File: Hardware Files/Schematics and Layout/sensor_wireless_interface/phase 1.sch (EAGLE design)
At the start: 6 parts, among them U1 RHD2216

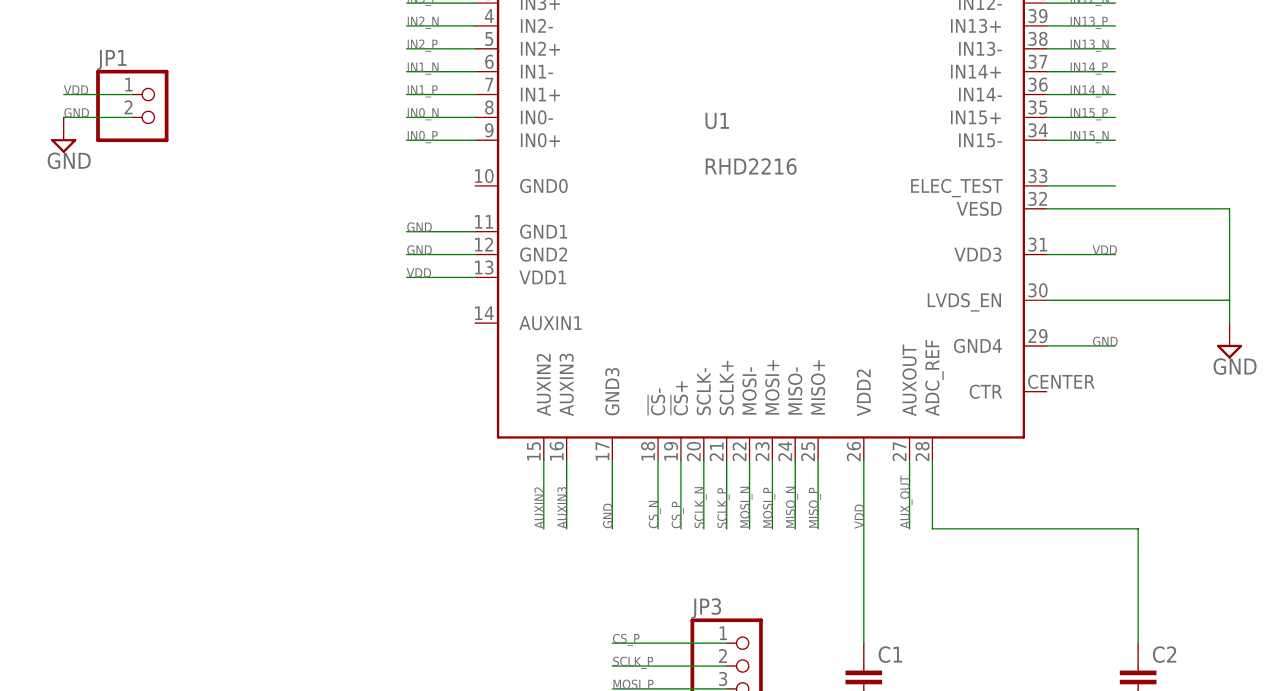
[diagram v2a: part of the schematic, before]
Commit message: added another pin header for AUXIN*
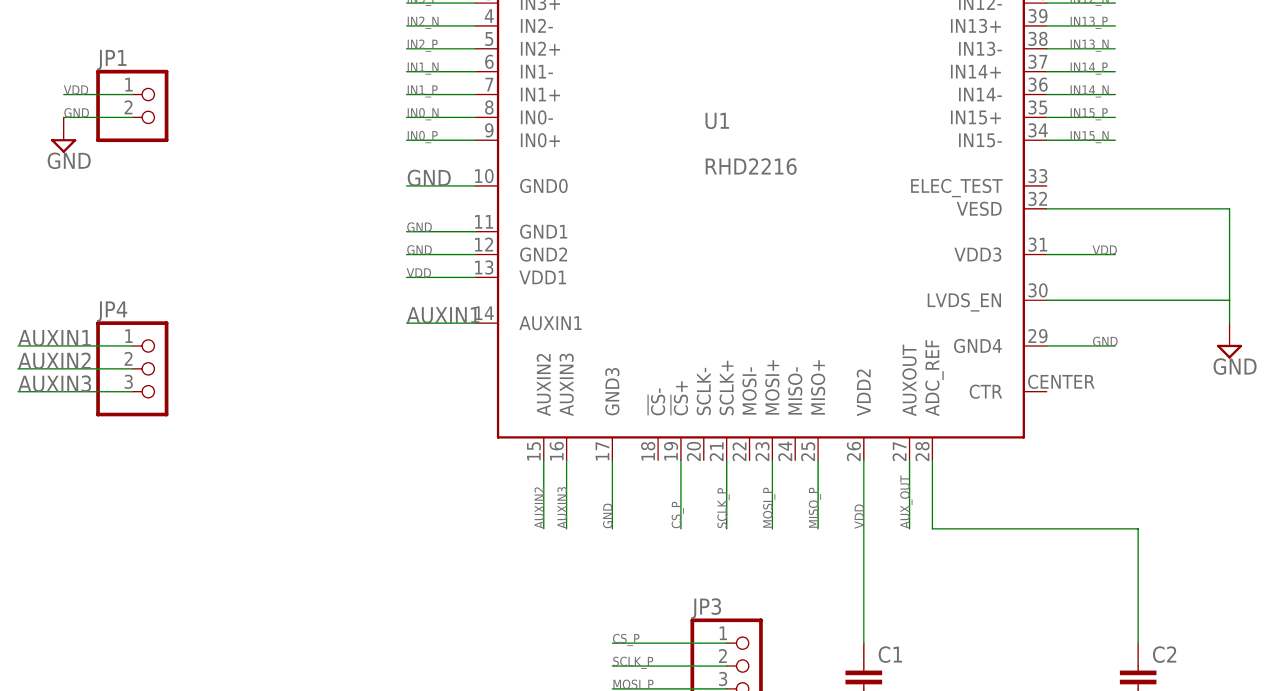
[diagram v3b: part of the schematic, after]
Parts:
- added JP4: (no value), pinhead:PINHD-1X3
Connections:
- removed net CS_N: U1.!CS!-
- removed net MISO_N: U1.MISO-
- removed net MOSI_N: U1.MOSI-
- removed net N$10: U1.ELEC_TEST
- removed net SCLK_N: U1.SCLK-
- new net AUXIN1: JP4.1, U1.AUXIN1
- net AUXIN2: now also JP4.2
- net AUXIN3: now also JP4.3
- net GND: now also U1.GND0
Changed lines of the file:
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@@
 <part name="C2" library="capacitor-wima" deviceset="C" device="2.5/2" value="10nF"/>
 <part name="SUPPLY4" library="supply2" deviceset="GND" device=""/>
+<part name="JP4" library="pinhead" deviceset="PINHD-1X3" device=""/>
 </parts>
 <sheets>
@@
 <instance part="C2" gate="G$1" x="10.16" y="35.56"/>
 <instance part="SUPPLY4" gate="GND" x="10.16" y="27.94"/>
+<instance part="JP4" gate="A" x="-99.06" y="68.58"/>
 </instances>
 <busses>
@@
 <pinref part="SUPPLY4" gate="GND" pin="GND"/>
 </segment>
+<segment>
+<pinref part="U1" gate="A" pin="GND0"/>
+<wire x1="-63.5" y1="88.9" x2="-71.12" y2="88.9" width="0.1524" layer="91"/>
+<label x="-71.12" y="88.9" size="1.778" layer="95"/>
+</segment>
 </net>
 <net name="AUXIN2" class="0">
@@
 <label x="-55.88" y="50.8" size="1.016" layer="95" rot="R90"/>
 </segment>
+<segment>
+<pinref part="JP4" gate="A" pin="2"/>
+<wire x1="-101.6" y1="68.58" x2="-114.3" y2="68.58" width="0.1524" layer="91"/>
+<label x="-114.3" y="68.58" size="1.778" layer="95"/>
+</segment>
 </net>
 <net name="AUXIN3" class="0">
@@
 <label x="-53.34" y="50.8" size="1.016" layer="95" rot="R90"/>
 </segment>
-</net>
-<net name="CS_N" class="0">
-<segment>
-<pinref part="U1" gate="A" pin="!CS!-"/>
-<wire x1="-43.18" y1="58.42" x2="-43.18" y2="50.8" width="0.1524" layer="91"/>
-<label x="-43.18" y="50.8" size="1.016" layer="95" rot="R90"/>
+<segment>
+<pinref part="JP4" gate="A" pin="3"/>
+<wire x1="-101.6" y1="66.04" x2="-114.3" y2="66.04" width="0.1524" layer="91"/>
+<label x="-114.3" y="66.04" size="1.778" layer="95"/>
 </segment>
 </net>
@@
 </segment>
 </net>
-<net name="SCLK_N" class="0">
-<segment>
-<pinref part="U1" gate="A" pin="SCLK-"/>
-<wire x1="-38.1" y1="58.42" x2="-38.1" y2="50.8" width="0.1524" layer="91"/>
-<label x="-38.1" y="50.8" size="1.016" layer="95" rot="R90"/>
-</segment>
-</net>
 <net name="SCLK_P" class="0">
 <segment>
@@
 </segment>
 </net>
-<net name="MOSI_N" class="0">
-<segment>
-<pinref part="U1" gate="A" pin="MOSI-"/>
-<wire x1="-33.02" y1="58.42" x2="-33.02" y2="50.8" width="0.1524" layer="91"/>
-<label x="-33.02" y="50.8" size="1.016" layer="95" rot="R90"/>
-</segment>
-</net>
 <net name="MOSI_P" class="0">
 <segment>
@@
 <wire x1="-35.56" y1="33.02" x2="-48.26" y2="33.02" width="0.1524" layer="91"/>
 <label x="-48.26" y="33.02" size="1.016" layer="95"/>
-</segment>
-</net>
-<net name="MISO_N" class="0">
-<segment>
-<pinref part="U1" gate="A" pin="MISO-"/>
-<wire x1="-27.94" y1="58.42" x2="-27.94" y2="50.8" width="0.1524" layer="91"/>
-<label x="-27.94" y="50.8" size="1.016" layer="95" rot="R90"/>
 </segment>
 </net>
@@
 <wire x1="71.12" y1="73.66" x2="83.82" y2="73.66" width="0.1524" layer="91"/>
 <label x="81.28" y="73.66" size="1.016" layer="95"/>
-</segment>
-</net>
-<net name="N$10" class="0">
-<segment>
-<pinref part="U1" gate="A" pin="ELEC_TEST"/>
-<wire x1="0" y1="88.9" x2="7.62" y2="88.9" width="0.1524" layer="91"/>
 </segment>
 </net>
@@
 </segment>
 </net>
+<net name="AUXIN1" class="0">
+<segment>
+<pinref part="JP4" gate="A" pin="1"/>
+<wire x1="-101.6" y1="71.12" x2="-114.3" y2="71.12" width="0.1524" layer="91"/>
+<label x="-114.3" y="71.12" size="1.778" layer="95"/>
+</segment>
+<segment>
+<pinref part="U1" gate="A" pin="AUXIN1"/>
+<wire x1="-63.5" y1="73.66" x2="-71.12" y2="73.66" width="0.1524" layer="91"/>
+<label x="-71.12" y="73.66" size="1.778" layer="95"/>
+</segment>
+</net>

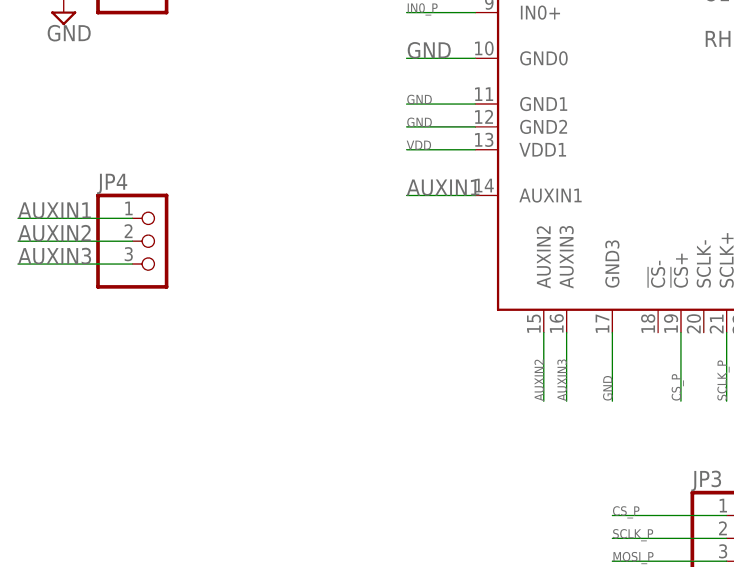
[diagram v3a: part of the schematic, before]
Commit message: connect AUXIN1-2-3 to VDD to save power
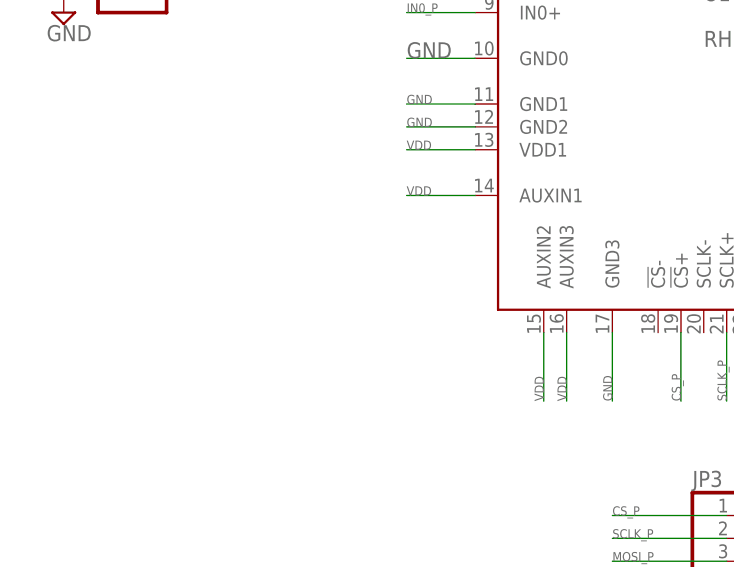
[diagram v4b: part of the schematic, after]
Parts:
- removed JP4: (no value), pinhead:PINHD-1X3
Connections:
- removed net AUXIN1: JP4.1, U1.AUXIN1
- removed net AUXIN2: JP4.2, U1.AUXIN2
- removed net AUXIN3: JP4.3, U1.AUXIN3
- net VDD: now also U1.AUXIN1, U1.AUXIN2, U1.AUXIN3
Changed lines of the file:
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@@
 <part name="C2" library="capacitor-wima" deviceset="C" device="2.5/2" value="10nF"/>
 <part name="SUPPLY4" library="supply2" deviceset="GND" device=""/>
-<part name="JP4" library="pinhead" deviceset="PINHD-1X3" device=""/>
 </parts>
 <sheets>
@@
 <instance part="C2" gate="G$1" x="10.16" y="35.56"/>
 <instance part="SUPPLY4" gate="GND" x="10.16" y="27.94"/>
-<instance part="JP4" gate="A" x="-99.06" y="68.58"/>
 </instances>
 <busses>
@@
 <wire x1="0" y1="81.28" x2="7.62" y2="81.28" width="0.1524" layer="91"/>
 <label x="5.08" y="81.28" size="1.016" layer="95"/>
+</segment>
+<segment>
+<pinref part="U1" gate="A" pin="AUXIN1"/>
+<wire x1="-63.5" y1="73.66" x2="-71.12" y2="73.66" width="0.1524" layer="91"/>
+<label x="-71.12" y="73.66" size="1.016" layer="95"/>
+</segment>
+<segment>
+<pinref part="U1" gate="A" pin="AUXIN2"/>
+<wire x1="-55.88" y1="58.42" x2="-55.88" y2="50.8" width="0.1524" layer="91"/>
+<label x="-55.88" y="50.8" size="1.016" layer="95" rot="R90"/>
+</segment>
+<segment>
+<pinref part="U1" gate="A" pin="AUXIN3"/>
+<wire x1="-53.34" y1="58.42" x2="-53.34" y2="50.8" width="0.1524" layer="91"/>
+<label x="-53.34" y="50.8" size="1.016" layer="95" rot="R90"/>
 </segment>
 </net>
@@
 </segment>
 </net>
-<net name="AUXIN2" class="0">
-<segment>
-<pinref part="U1" gate="A" pin="AUXIN2"/>
-<wire x1="-55.88" y1="58.42" x2="-55.88" y2="50.8" width="0.1524" layer="91"/>
-<label x="-55.88" y="50.8" size="1.016" layer="95" rot="R90"/>
-</segment>
-<segment>
-<pinref part="JP4" gate="A" pin="2"/>
-<wire x1="-101.6" y1="68.58" x2="-114.3" y2="68.58" width="0.1524" layer="91"/>
-<label x="-114.3" y="68.58" size="1.778" layer="95"/>
-</segment>
-</net>
-<net name="AUXIN3" class="0">
-<segment>
-<pinref part="U1" gate="A" pin="AUXIN3"/>
-<wire x1="-53.34" y1="58.42" x2="-53.34" y2="50.8" width="0.1524" layer="91"/>
-<label x="-53.34" y="50.8" size="1.016" layer="95" rot="R90"/>
-</segment>
-<segment>
-<pinref part="JP4" gate="A" pin="3"/>
-<wire x1="-101.6" y1="66.04" x2="-114.3" y2="66.04" width="0.1524" layer="91"/>
-<label x="-114.3" y="66.04" size="1.778" layer="95"/>
-</segment>
-</net>
 <net name="CS_P" class="0">
 <segment>
@@
 </segment>
 </net>
-<net name="AUXIN1" class="0">
-<segment>
-<pinref part="JP4" gate="A" pin="1"/>
-<wire x1="-101.6" y1="71.12" x2="-114.3" y2="71.12" width="0.1524" layer="91"/>
-<label x="-114.3" y="71.12" size="1.778" layer="95"/>
-</segment>
-<segment>
-<pinref part="U1" gate="A" pin="AUXIN1"/>
-<wire x1="-63.5" y1="73.66" x2="-71.12" y2="73.66" width="0.1524" layer="91"/>
-<label x="-71.12" y="73.66" size="1.778" layer="95"/>
-</segment>
-</net>
